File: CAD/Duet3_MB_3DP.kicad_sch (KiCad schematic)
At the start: 0 parts

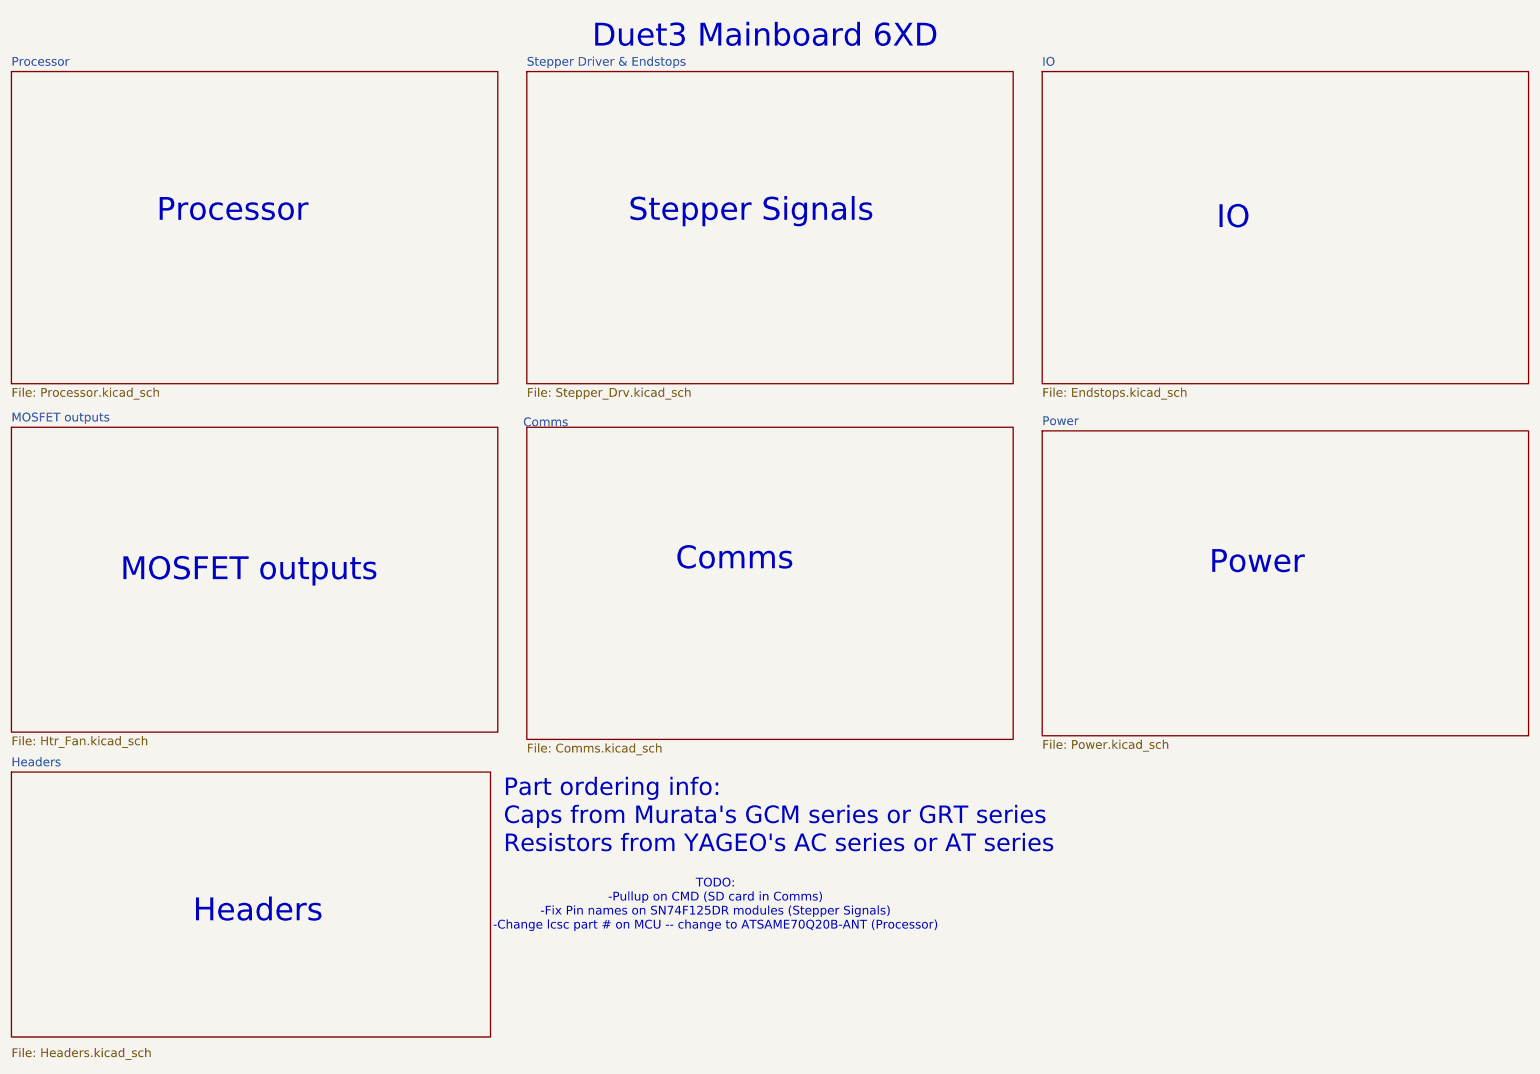
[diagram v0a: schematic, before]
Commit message: WIP redoing board for new print
Removed version resistors.
Added pull-up on CMD.
Working on motors, not routed.
Added local library for custom parts.
Ran auto-cleanup of traces and vias (supervised).
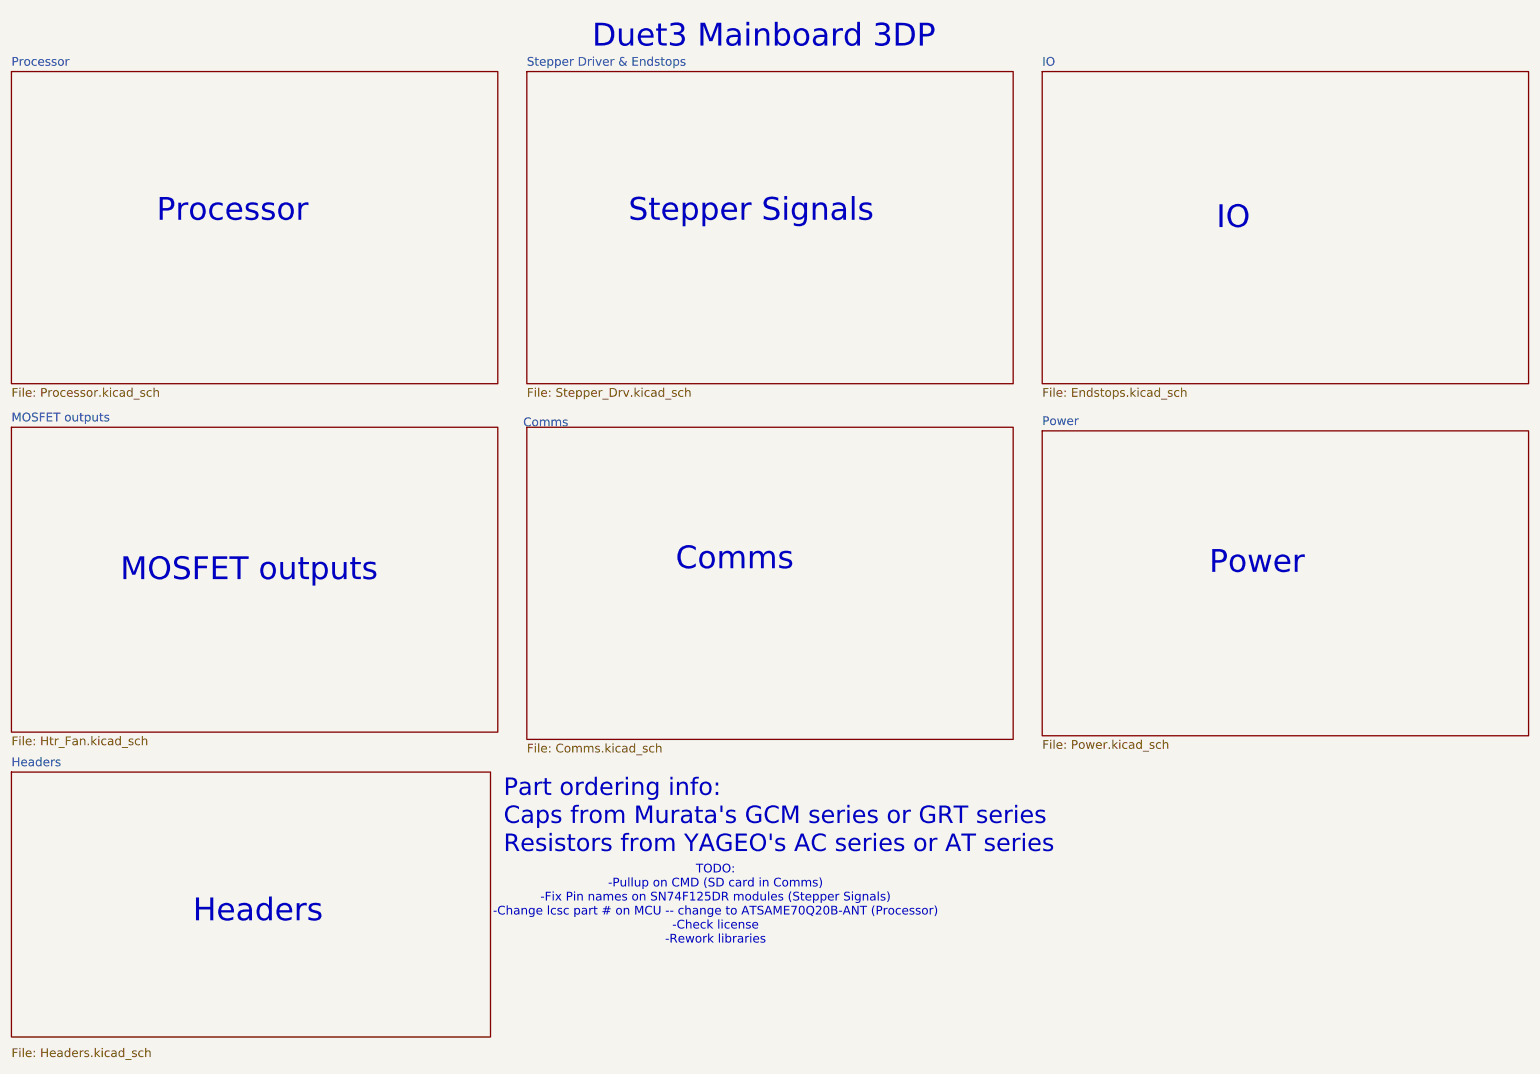
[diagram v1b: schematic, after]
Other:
- note added: "Duet3 Mainboard 3DP"
- note added: "TODO: -Pullup on CMD (SD card in Comms) -Fix Pin names on SN74F125DR modules (Stepper Signals) -Change lcsc part # on MCU -- change to ATSAME70Q20B-ANT (Processor) -Check license -Rework libraries"
- note removed: "Duet3 Mainboard 6XD"
- note removed: "TODO: -Pullup on CMD (SD card in Comms) -Fix Pin names on SN74F125DR modules (Stepper Signals) -Change lcsc part # on MCU -- change to ATSAME70Q20B-ANT (Processor)"
- company: Duet3d -> 3DPotter
- title: Duet 3 Main Board 6XD -> Duet 3 Main Board 3DP
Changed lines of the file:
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@@
 (kicad_sch
-	(version 20231120)
+	(version 20250114)
 	(generator "eeschema")
-	(generator_version "8.0")
+	(generator_version "9.0")
 	(paper "A4")
 	(title_block
-		(title "Duet 3 Main Board 6XD")
+		(title "Duet 3 Main Board 3DP")
 		(date "2023-02-22")
-		(rev "1.01")
-		(company "Duet3d")
-		(comment 1 "(c) Duet3D")
-	)
-	(text "TODO:\n-Pullup on CMD (SD card in Comms)\n-Fix Pin names on SN74F125DR modules (Stepper Signals)\n-Change lcsc part # on MCU -- change to ATSAME70Q20B-ANT (Processor)"
+		(rev "1.0")
+		(company "3DPotter")
+		(comment 1 "(c) 3DPotter")
+	)
+	(text "TODO:\n-Pullup on CMD (SD card in Comms)\n-Fix Pin names on SN74F125DR modules (Stepper Signals)\n-Change lcsc part # on MCU -- change to ATSAME70Q20B-ANT (Processor)\n-Check license\n-Rework libraries"
 		(exclude_from_sim no)
 		(at 138.43 168.656 0)
@@
 		)
 	)
-	(text "Duet3 Mainboard 6XD"
+	(text "Duet3 Mainboard 3DP"
 		(exclude_from_sim no)
 		(at 116.84 19.05 0)
@@
 		(at 15.24 22.86)
 		(size 85.09 54.61)
+		(exclude_from_sim no)
+		(in_bom yes)
+		(on_board yes)
+		(dnp no)
 		(fields_autoplaced yes)
 		(stroke
@@
 		)
 		(instances
-			(project "Duet3_MB_6XD"
+			(project "Duet3_MB_3DP"
 				(path "/94813053-1316-4754-9fb4-4dbbf7dc780d"
 					(page "1")
@@
 		(at 105.41 22.86)
 		(size 85.09 54.61)
+		(exclude_from_sim no)
+		(in_bom yes)
+		(on_board yes)
+		(dnp no)
 		(fields_autoplaced yes)
 		(stroke
@@
 		)
 		(instances
-			(project "Duet3_MB_6XD"
+			(project "Duet3_MB_3DP"
 				(path "/94813053-1316-4754-9fb4-4dbbf7dc780d"
 					(page "2")
@@
 		(at 195.58 85.725)
 		(size 85.09 53.34)
+		(exclude_from_sim no)
+		(in_bom yes)
+		(on_board yes)
+		(dnp no)
 		(fields_autoplaced yes)
 		(stroke
@@
 		)
 		(instances
-			(project "Duet3_MB_6XD"
+			(project "Duet3_MB_3DP"
 				(path "/94813053-1316-4754-9fb4-4dbbf7dc780d"
 					(page "6")
@@
 		(at 15.24 145.415)
 		(size 83.82 46.355)
+		(exclude_from_sim no)
+		(in_bom yes)
+		(on_board yes)
+		(dnp no)
 		(stroke
 			(width 0)
@@
 		)
 		(instances
-			(project "Duet3_MB_6XD"
+			(project "Duet3_MB_3DP"
 				(path "/94813053-1316-4754-9fb4-4dbbf7dc780d"
 					(page "7")
@@
 		(at 15.24 85.09)
 		(size 85.09 53.34)
+		(exclude_from_sim no)
+		(in_bom yes)
+		(on_board yes)
+		(dnp no)
 		(fields_autoplaced yes)
 		(stroke
@@
 		)
 		(instances
-			(project "Duet3_MB_6XD"
+			(project "Duet3_MB_3DP"
 				(path "/94813053-1316-4754-9fb4-4dbbf7dc780d"
 					(page "4")
@@
 		(at 105.41 85.09)
 		(size 85.09 54.61)
+		(exclude_from_sim no)
+		(in_bom yes)
+		(on_board yes)
+		(dnp no)
 		(stroke
 			(width 0)
@@
 		)
 		(instances
-			(project "Duet3_MB_6XD"
+			(project "Duet3_MB_3DP"
 				(path "/94813053-1316-4754-9fb4-4dbbf7dc780d"
 					(page "5")
@@
 		(at 195.58 22.86)
 		(size 85.09 54.61)
+		(exclude_from_sim no)
+		(in_bom yes)
+		(on_board yes)
+		(dnp no)
 		(fields_autoplaced yes)
 		(stroke
@@
 		)
 		(instances
-			(project "Duet3_MB_6XD"
+			(project "Duet3_MB_3DP"
 				(path "/94813053-1316-4754-9fb4-4dbbf7dc780d"
 					(page "3")
@@
 		)
 	)
+	(embedded_fonts no)
 )

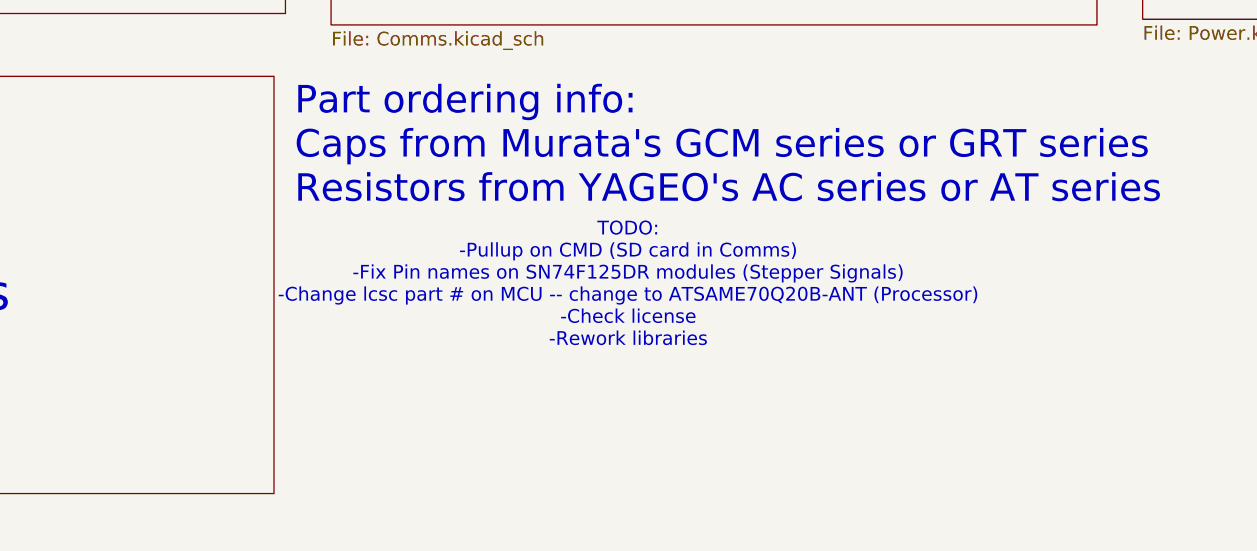
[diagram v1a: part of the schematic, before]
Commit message: motors have been routed
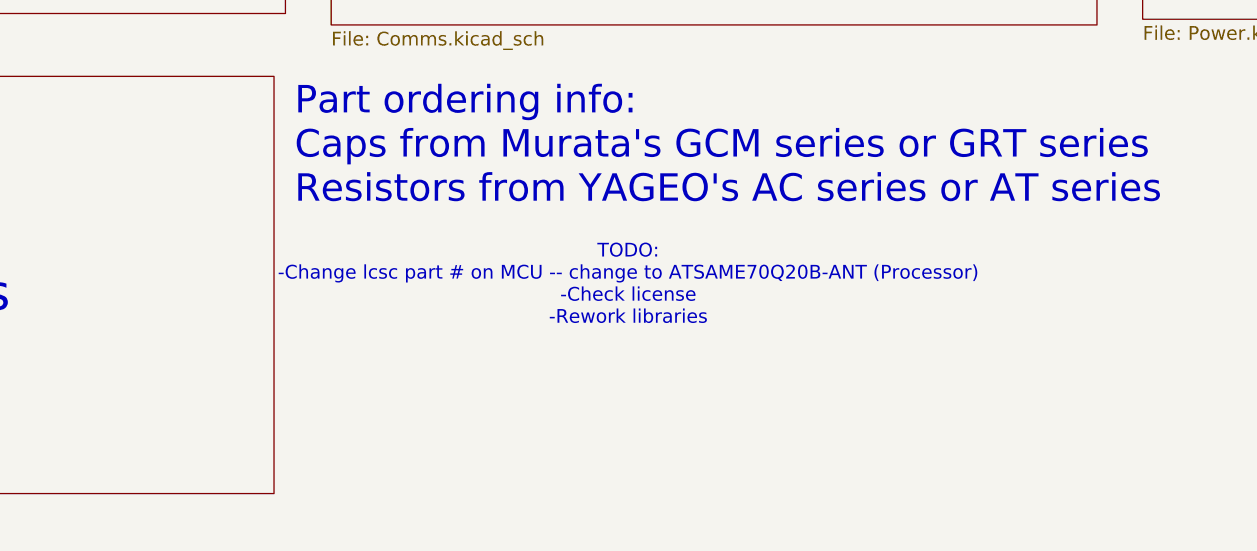
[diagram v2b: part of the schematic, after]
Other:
- note added: "TODO: -Change lcsc part # on MCU -- change to ATSAME70Q20B-ANT (Processor) -Check license -Rework libraries"
- note removed: "TODO: -Pullup on CMD (SD card in Comms) -Fix Pin names on SN74F125DR modules (Stepper Signals) -Change lcsc part # on MCU -- change to ATSAME70Q20B-ANT (Processor) -Check license -Rework libraries"
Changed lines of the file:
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@@
 		(comment 1 "(c) 3DPotter")
 	)
-	(text "TODO:\n-Pullup on CMD (SD card in Comms)\n-Fix Pin names on SN74F125DR modules (Stepper Signals)\n-Change lcsc part # on MCU -- change to ATSAME70Q20B-ANT (Processor)\n-Check license\n-Rework libraries"
+	(text "TODO:\n-Change lcsc part # on MCU -- change to ATSAME70Q20B-ANT (Processor)\n-Check license\n-Rework libraries"
 		(exclude_from_sim no)
 		(at 138.43 168.656 0)

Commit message: update processor order info
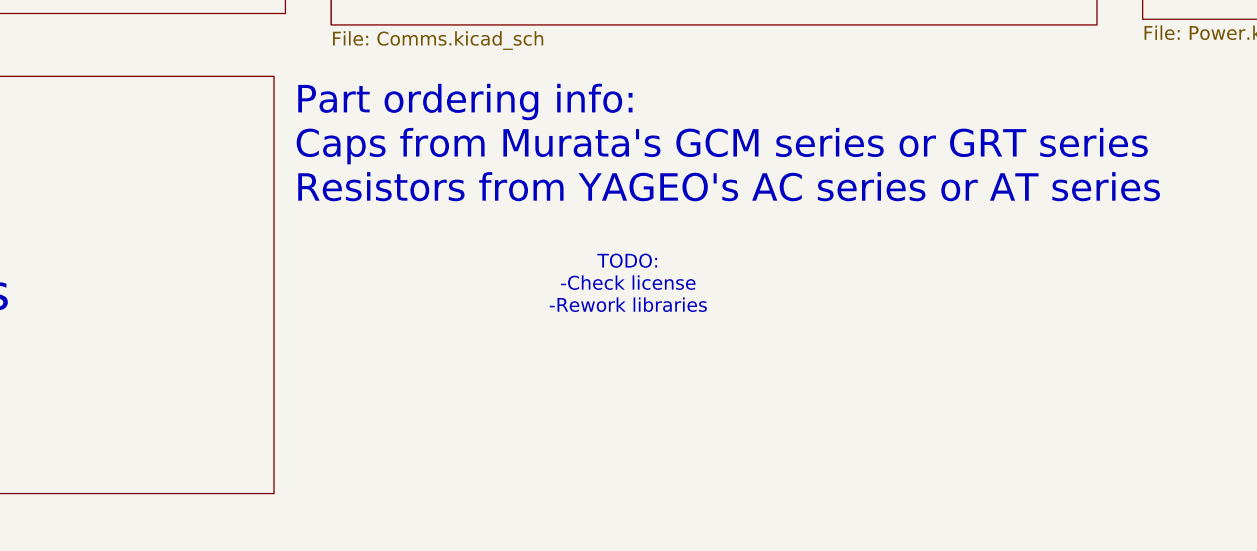
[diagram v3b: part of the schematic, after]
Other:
- note added: "TODO: -Check license -Rework libraries"
- note removed: "TODO: -Change lcsc part # on MCU -- change to ATSAME70Q20B-ANT (Processor) -Check license -Rework libraries"
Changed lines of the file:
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@@
 		(comment 1 "(c) 3DPotter")
 	)
-	(text "TODO:\n-Change lcsc part # on MCU -- change to ATSAME70Q20B-ANT (Processor)\n-Check license\n-Rework libraries"
+	(text "TODO:\n-Check license\n-Rework libraries"
 		(exclude_from_sim no)
 		(at 138.43 168.656 0)

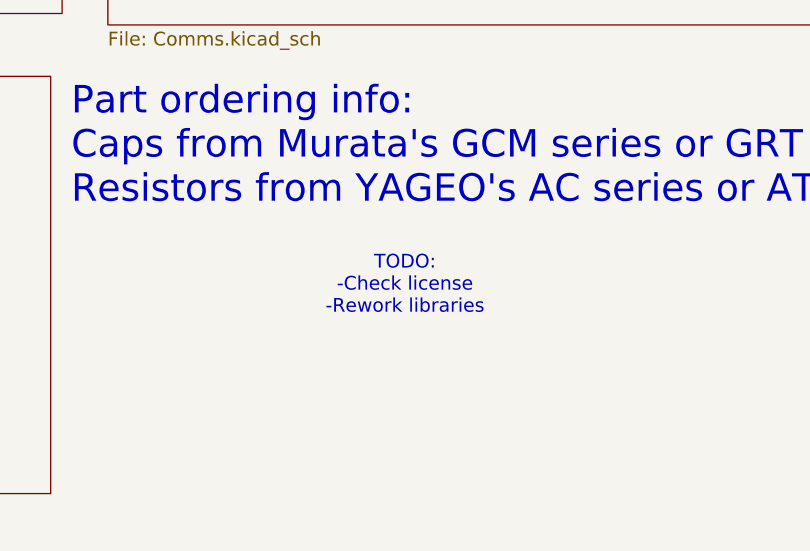
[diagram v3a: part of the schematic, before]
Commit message: TODO: Finish LM5013, find replacement for TS30041
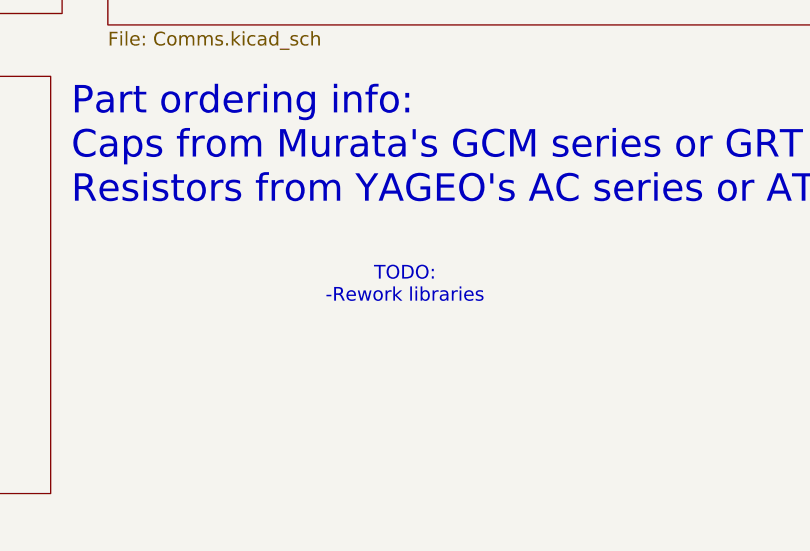
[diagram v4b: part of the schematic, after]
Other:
- note added: "TODO: -Rework libraries"
- note removed: "TODO: -Check license -Rework libraries"
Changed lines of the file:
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@@
 		(comment 1 "(c) 3DPotter")
 	)
-	(text "TODO:\n-Check license\n-Rework libraries"
+	(text "TODO:\n-Rework libraries"
 		(exclude_from_sim no)
 		(at 138.43 168.656 0)
